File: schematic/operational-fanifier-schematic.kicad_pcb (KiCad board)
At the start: 2 copper layers, 19 parts, among them J1 Conn_01x03, M1 Fan, Q1 BC337, Q2 BC337, SW1 SW_SPDT, U1 LM324N, U2 74HC32, U3 LM335Z

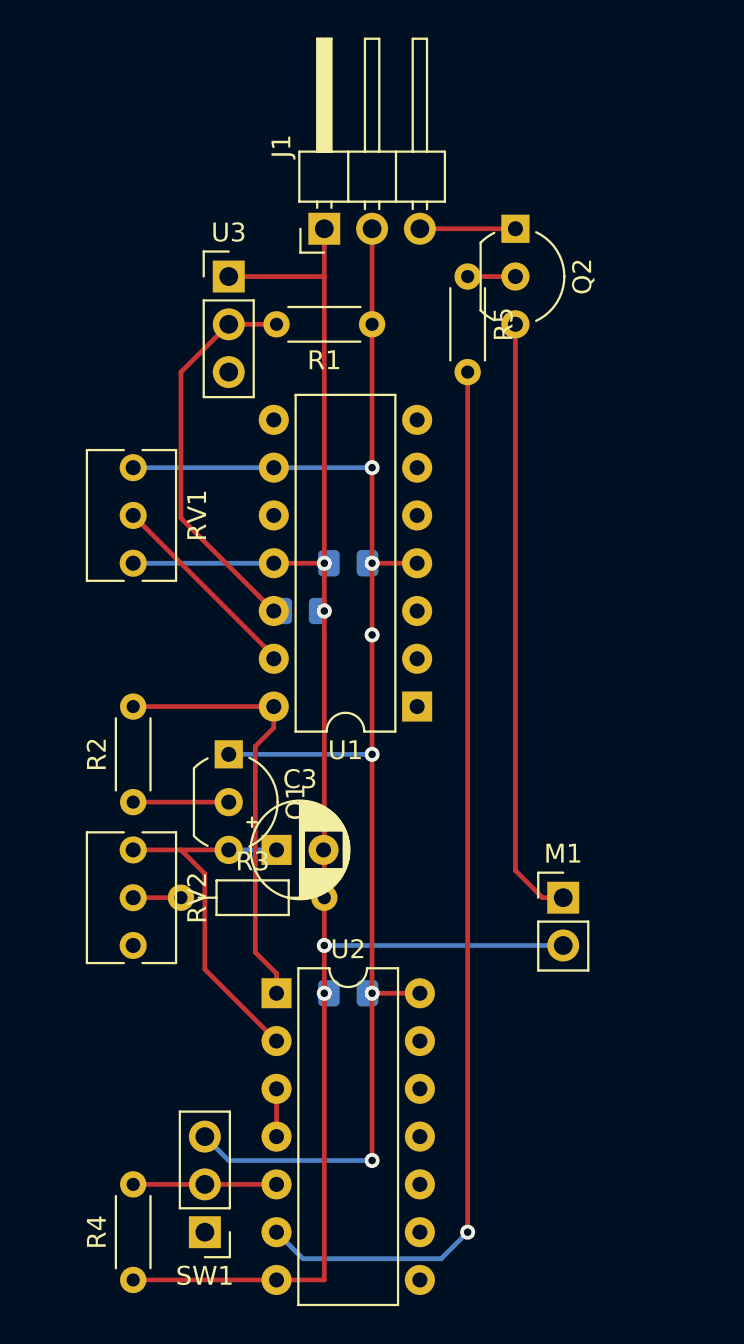
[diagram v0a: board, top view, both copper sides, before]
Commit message: Move the transistor to below the fan. Add test results with transistored
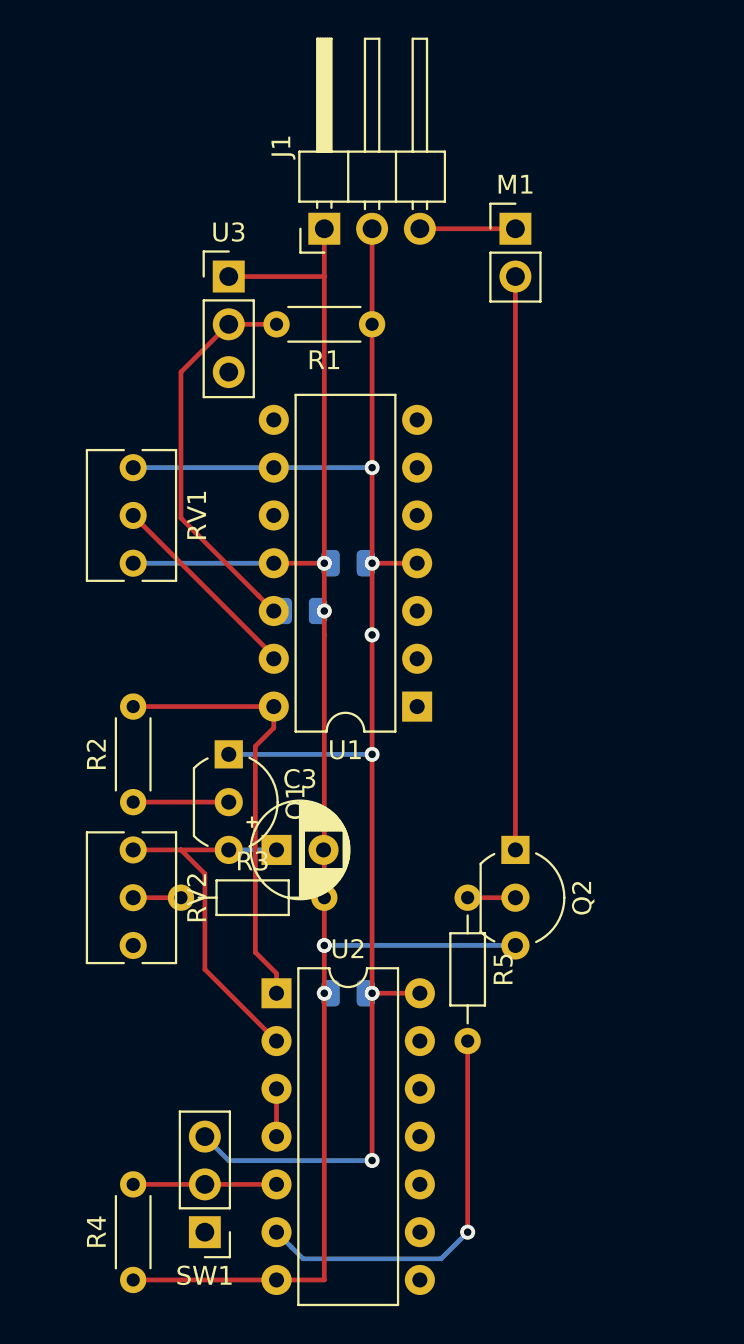
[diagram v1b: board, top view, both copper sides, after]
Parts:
- C1, C2: footprint Capacitor_SMD:C_0805_2012Metric_Pad1.15x1.40mm_HandSolder -> Capacitor_SMD:C_0805_2012Metric
- R5: footprint Resistor_THT:R_Axial_DIN0204_L3.6mm_D1.6mm_P5.08mm_Horizontal -> Resistor_THT:R_Axial_DIN0204_L3.6mm_D1.6mm_P7.62mm_Horizontal
- moved M1 35.7 mm to (158.8, 25.4)
- moved Q2 33.0 mm to (158.8, 58.4)
- moved R5 33.0 mm to (156.2, 61.0)
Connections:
- M1 pad 1: Net-(M1-Pad1) -> +12V
- M1 pad 2: GND -> Net-(M1-Pad2)
- Q2 pad 1: +12V -> Net-(M1-Pad2)
- Q2 pad 3: Net-(M1-Pad1) -> GND
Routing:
- net Net-(R5-Pad2): track 57.1 -> 21.5 mm
- net Net-(M1-Pad1): track 32.2 -> 0.00 mm
- net Net-(M1-Pad2): track 0.00 -> 30.5 mm
- net GND: track 94.0 -> 91.4 mm

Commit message: Use two-pin footprints where applicable. Use horizontal headers for M1 and U3
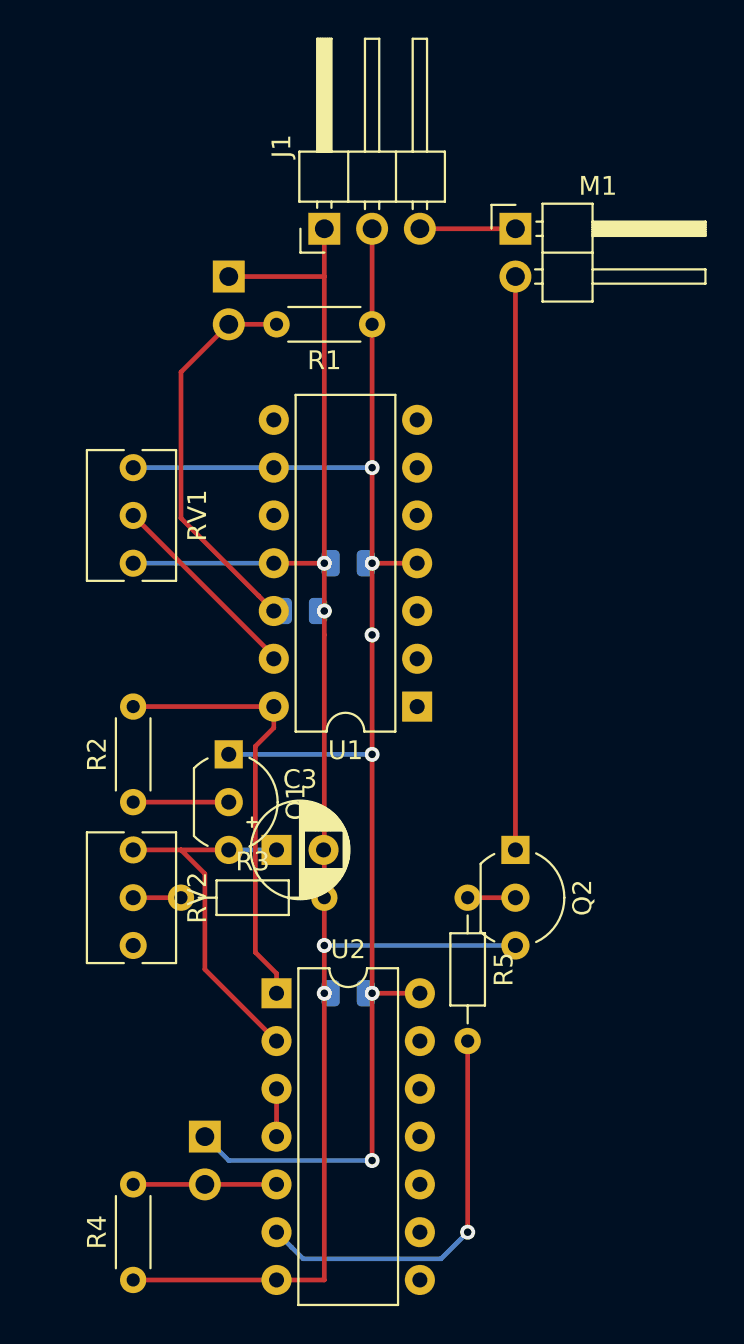
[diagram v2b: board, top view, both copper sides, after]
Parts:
- M1: footprint Connector_PinHeader_2.54mm:PinHeader_1x02_P2.54mm_Vertical -> Connector_PinHeader_2.54mm:PinHeader_1x02_P2.54mm_Horizontal
- SW1: footprint Connector_PinHeader_2.54mm:PinHeader_1x03_P2.54mm_Vertical -> Connector_PinHeader_2.54mm:PinHeader_1x02_P2.54mm_Vertical; moved to B.Cu
- U3: footprint Connector_PinHeader_2.54mm:PinHeader_1x03_P2.54mm_Vertical -> Connector_PinHeader_2.54mm:PinHeader_1x02_P2.54mm_Horizontal; moved to B.Cu
- moved SW1 5.08 mm to (142.2, 73.7)
- turned U3 to 180 degrees

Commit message: Don't flip when not required
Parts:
- SW1, U3: moved to F.Cu
- moved SW1 2.54 mm to (142.2, 76.2)
- moved U3 2.54 mm to (143.5, 30.5)
